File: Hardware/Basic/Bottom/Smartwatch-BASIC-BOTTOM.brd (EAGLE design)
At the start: 33 x 33 mm, 37 parts, among them U1 AD5242-SO16, U3 PCF8523

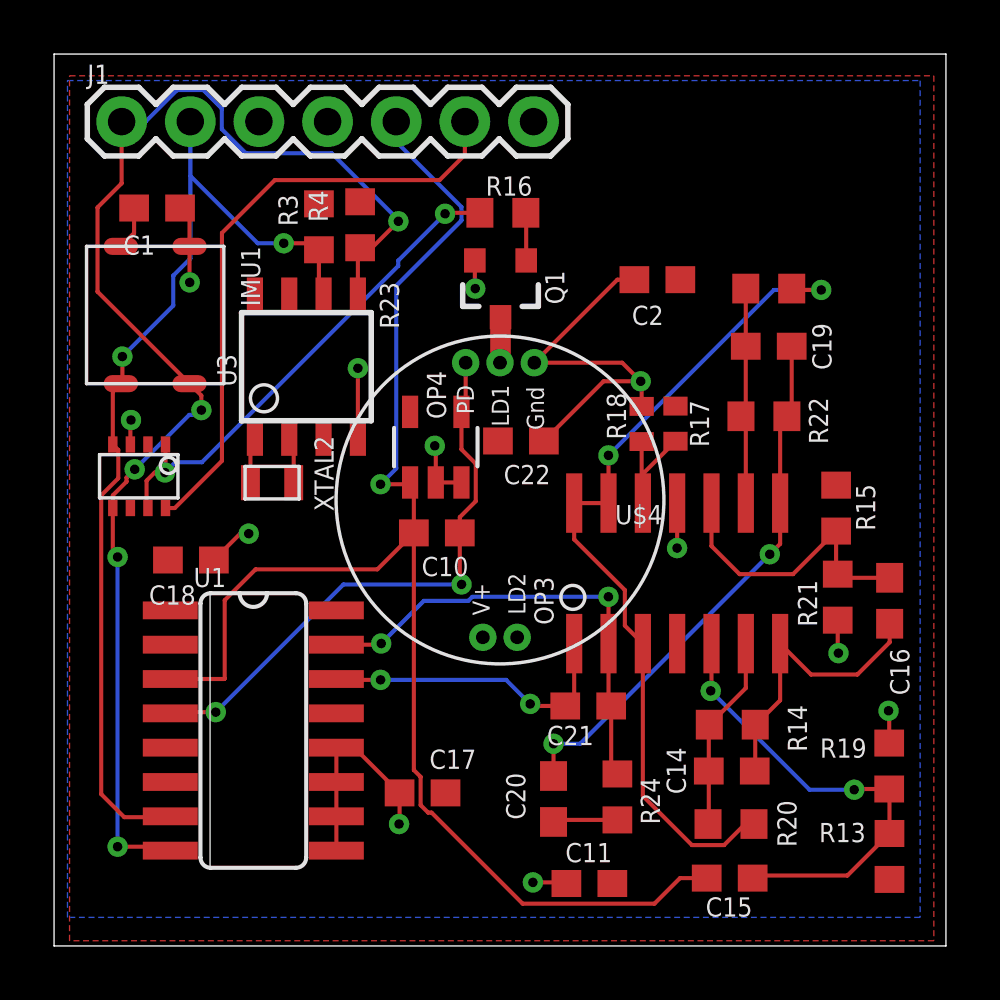
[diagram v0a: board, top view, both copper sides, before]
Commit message: Header Pins Fixed
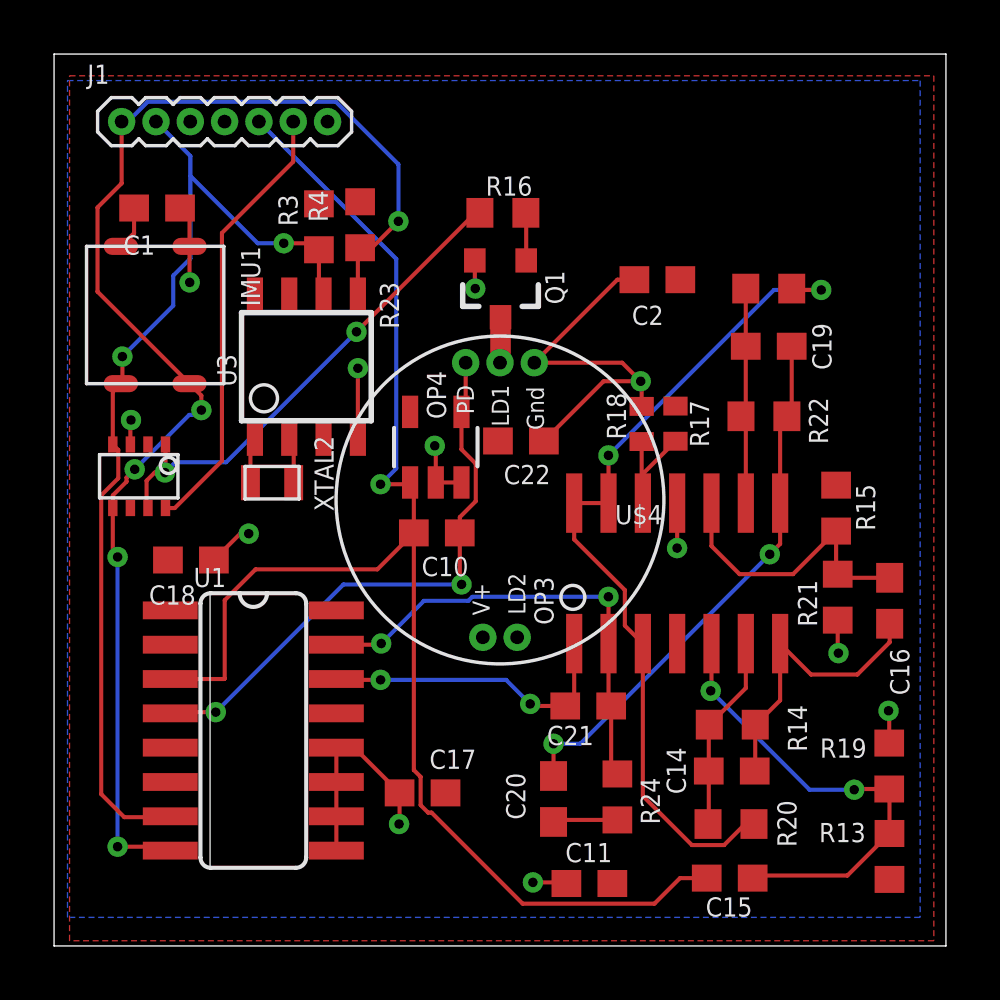
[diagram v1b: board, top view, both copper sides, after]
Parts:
- J1: device LinnesLab-Connectors:1X07 -> LinnesLab-Connectors:1X07_1.27MM
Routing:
- net D26/LED.CTRL: track 22.7 -> 16.5 mm
- net SCL: track 37.0 -> 37.5 mm
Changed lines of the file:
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@@
 <attribute name="VALUE" x="15.3926" y="22.0282" size="0.7112" layer="27" rot="R90"/>
 </element>
-<element name="J1" library="LinnesLab-Connectors" package="1X07" value="" x="5" y="33" smashed="yes">
+<element name="J1" library="LinnesLab-Connectors" package="1X07_1.27MM" value="" x="5" y="33" smashed="yes">
 <attribute name="NAME" x="3.73" y="34.397" size="0.7112" layer="25" font="vector" ratio="20"/>
 <attribute name="VALUE" x="3.73" y="30.968" size="0.6096" layer="27" font="vector" ratio="20"/>
@@
 <wire x1="5.4838" y1="20.13415" x2="7.49845" y2="22.1488" width="0.1524" layer="16"/>
 <wire x1="7.49845" y1="22.1488" x2="7.7724" y2="22.1488" width="0.1524" layer="16"/>
-<wire x1="15.24" y1="29.3116" x2="15.24" y2="29.3624" width="0.1524" layer="16"/>
-<wire x1="15.24" y1="29.3624" x2="12.7708" y2="31.8316" width="0.1524" layer="16"/>
-<wire x1="8.7084" y1="33.48396875" x2="8.02396875" y2="34.1684" width="0.1524" layer="16"/>
-<wire x1="8.02396875" y1="34.1684" x2="7.05603125" y2="34.1684" width="0.1524" layer="16"/>
-<wire x1="5.88763125" y1="33" x2="5" y2="33" width="0.1524" layer="16"/>
-<wire x1="7.05603125" y1="34.1684" x2="5.88763125" y2="33" width="0.1524" layer="16"/>
-<wire x1="9.59603125" y1="31.8316" x2="8.7084" y2="32.71923125" width="0.1524" layer="16"/>
-<wire x1="8.7084" y1="32.71923125" x2="8.7084" y2="33.48396875" width="0.1524" layer="16"/>
-<wire x1="12.7708" y1="31.8316" x2="9.59603125" y2="31.8316" width="0.1524" layer="16"/>
+<wire x1="5" y1="33" x2="5.2282875" y2="33" width="0.1524" layer="16"/>
+<wire x1="5.2282875" y1="33" x2="5.9648875" y2="33.7366" width="0.1524" layer="16"/>
+<wire x1="5.9648875" y1="33.7366" x2="12.9251125" y2="33.7366" width="0.1524" layer="16"/>
+<wire x1="12.9251125" y1="33.7366" x2="15.24" y2="31.4217125" width="0.1524" layer="16"/>
+<wire x1="15.24" y1="31.4217125" x2="15.24" y2="29.3116" width="0.1524" layer="16"/>
 </signal>
 <signal name="SCL">
@@
 <wire x1="6.7676" y1="7.2644" x2="6.7996" y2="7.2964" width="0.1524" layer="1"/>
 <wire x1="7.5438" y1="27.93455" x2="7.5438" y2="30.988" width="0.1524" layer="16"/>
-<wire x1="7.5438" y1="30.988" x2="7.5438" y2="32.9962" width="0.1524" layer="16"/>
-<wire x1="7.5438" y1="32.9962" x2="7.54" y2="33" width="0.1524" layer="16"/>
 <wire x1="10.033" y1="28.4988" x2="7.5438" y2="30.988" width="0.1524" layer="16"/>
 <wire x1="10.033" y1="28.4988" x2="10.9982" y2="28.4988" width="0.1524" layer="16"/>
@@
 <wire x1="12.2238" y1="28.2582" x2="12.3" y2="28.2582" width="0.1524" layer="1"/>
 <wire x1="12.2238" y1="28.2582" x2="11.9832" y2="28.4988" width="0.1524" layer="1"/>
+<wire x1="7.5438" y1="30.988" x2="7.5438" y2="31.7262" width="0.1524" layer="16"/>
+<wire x1="7.5438" y1="31.7262" x2="6.27" y2="33" width="0.1524" layer="16"/>
 </signal>
 <signal name="A6/TIA">
@@
 <wire x1="8.8138" y1="12.3952" x2="8.795" y2="12.3764" width="0.1524" layer="1"/>
 <wire x1="8.795" y1="12.3764" x2="6.7996" y2="12.3764" width="0.1524" layer="1"/>
-<wire x1="15.1638" y1="20.1676" x2="14.5796" y2="19.5834" width="0.1524" layer="16"/>
+<wire x1="14.5796" y1="19.5834" x2="15.1638" y2="20.1676" width="0.1524" layer="16"/>
 <via x="14.5796" y="19.5834" extent="1-16" drill="0.35"/>
-<wire x1="17.574" y1="29.33965" x2="17.574" y2="29.84235" width="0.1524" layer="16"/>
-<wire x1="15.1638" y1="26.92945" x2="15.1638" y2="20.1676" width="0.1524" layer="16"/>
-<wire x1="17.574" y1="29.33965" x2="15.1638" y2="26.92945" width="0.1524" layer="16"/>
 <wire x1="14.5796" y1="19.5834" x2="15.6084" y2="19.5834" width="0.1524" layer="1"/>
 <wire x1="15.6084" y1="19.5834" x2="15.674" y2="19.649" width="0.1524" layer="1"/>
-<wire x1="15.16" y1="32.25635" x2="15.16" y2="33" width="0.1524" layer="16"/>
-<wire x1="17.574" y1="29.84235" x2="15.16" y2="32.25635" width="0.1524" layer="16"/>
+<wire x1="15.1638" y1="27.9162" x2="10.08" y2="33" width="0.1524" layer="16"/>
+<wire x1="15.1638" y1="20.1676" x2="15.1638" y2="27.9162" width="0.1524" layer="16"/>
 </signal>
 <signal name="PD.C">
@@
 <contactref element="U$4" pad="1"/>
 <contactref element="R16" pad="1"/>
-<wire x1="18.2564" y1="29.6258" x2="17.002" y2="29.6258" width="0.1524" layer="1"/>
-<wire x1="17.002" y1="29.6258" x2="16.9672" y2="29.591" width="0.1524" layer="1"/>
-<via x="16.9672" y="29.591" extent="1-16" drill="0.35"/>
 <via x="6.604" y="20.0152" extent="1-16" drill="0.35"/>
-<wire x1="16.9672" y1="29.591" x2="15.2372" y2="27.861" width="0.1524" layer="16"/>
-<wire x1="15.2372" y1="27.861" x2="15.2372" y2="27.66325" width="0.1524" layer="16"/>
-<wire x1="15.2372" y1="27.66325" x2="7.97015" y2="20.3962" width="0.1524" layer="16"/>
-<wire x1="7.97015" y1="20.3962" x2="6.985" y2="20.3962" width="0.1524" layer="16"/>
 <wire x1="6.604" y1="20.0152" x2="6.985" y2="20.3962" width="0.1524" layer="16"/>
 <wire x1="6.604" y1="20.0152" x2="6.6238" y2="20.035" width="0.1524" layer="1"/>
@@
 <wire x1="5.923" y1="19.7152" x2="5.923" y2="18.7532" width="0.1524" layer="1"/>
 <wire x1="5.923" y1="18.7532" x2="5.9738" y2="18.7024" width="0.1524" layer="1"/>
+<wire x1="8.8646" y1="20.3962" x2="13.6906" y2="25.2222" width="0.1524" layer="16"/>
+<via x="13.6906" y="25.2222" extent="1-16" drill="0.35"/>
+<wire x1="6.985" y1="20.3962" x2="8.8646" y2="20.3962" width="0.1524" layer="16"/>
+<wire x1="13.6906" y1="25.2222" x2="18.0942" y2="29.6258" width="0.1524" layer="1"/>
+<wire x1="18.0942" y1="29.6258" x2="18.2564" y2="29.6258" width="0.1524" layer="1"/>
 </signal>
 <signal name="N$10">
@@
 <contactref element="J1" pad="6"/>
 <contactref element="U$4" pad="8"/>
-<wire x1="17.7" y1="33" x2="17.7" y2="31.7716" width="0.1524" layer="1"/>
-<wire x1="17.7" y1="31.7716" x2="16.764" y2="30.8356" width="0.1524" layer="1"/>
-<wire x1="16.764" y1="30.8356" x2="10.668" y2="30.8356" width="0.1524" layer="1"/>
-<wire x1="10.668" y1="30.8356" x2="8.7122" y2="28.8798" width="0.1524" layer="1"/>
-<wire x1="8.7122" y1="28.8798" x2="8.7122" y2="20.447" width="0.1524" layer="1"/>
+<wire x1="8.7122" y1="20.447" x2="8.7122" y2="28.8798" width="0.1524" layer="1"/>
 <wire x1="8.7122" y1="20.447" x2="6.9676" y2="18.7024" width="0.1524" layer="1"/>
 <wire x1="6.9676" y1="18.7024" x2="6.6238" y2="18.7024" width="0.1524" layer="1"/>
+<wire x1="11.35" y1="31.5176" x2="11.35" y2="33" width="0.1524" layer="1"/>
+<wire x1="8.7122" y1="28.8798" x2="11.35" y2="31.5176" width="0.1524" layer="1"/>
 </signal>
 </signals>

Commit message: GPS Removed, added back original display, kept pads for adafruit display
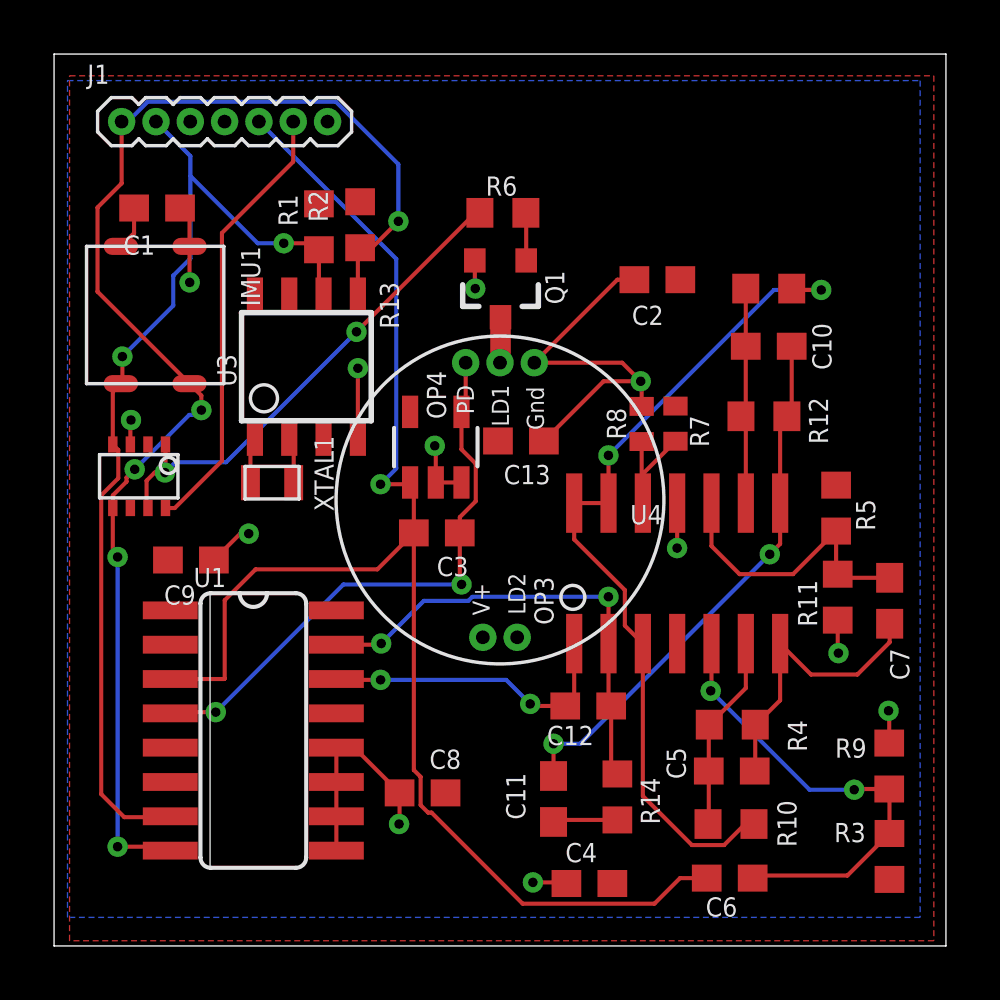
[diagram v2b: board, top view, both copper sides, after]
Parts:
- removed C19: 2.2n, LinnesLab-Passives:C0603
- removed C20: 22u, LinnesLab-Passives:C0603
- removed R23: 1M, LinnesLab-Passives:R0603
- removed R24: 10k, LinnesLab-Passives:R0603
- added C3, C4: 100n, LinnesLab-Passives:C0603
- added R1, R2: 10k, LinnesLab-Passives:R0603
- C10: value 100n -> 2.2n
- C11: value 100n -> 22u
- R13: value 220k -> 1M
- R14: value 10M -> 10k
- R3: value 10k -> 220k
- R4: value 10k -> 10M
- moved R3 31.4 mm to (33.4, 5.81), turned to 270 degrees
- moved R4 23.1 mm to (27.6, 10.7), turned to 0 degrees
- moved R13 21.5 mm to (28.9, 26.8), turned to 180 degrees
- moved C10 14.1 mm to (28.9, 24.7)
- moved R14 5.02 mm to (23.3, 8.01), turned to 270 degrees
- moved C11 3.40 mm to (21.0, 7.94), turned to 270 degrees
- renumbered C14 to C5, C15 to C6, C16 to C7, C17 to C8, C18 to C9, C21 to C12, C22 to C13, R15 to R5, R16 to R6, R17 to R7, R18 to R8, R19 to R9, R20 to R10, R21 to R11, R22 to R12, U$3 to U2, U$4 to U4, XTAL2 to XTAL1
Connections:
- net 3.3V: now also C4.2, R1.2, R2.2; no longer C11.2, R13.2, R4.2
- net A6/TIA: now also C3.2; no longer C10.2
- net G.W2: now also R14.1; no longer R24.1
- net GND: now also C4.1; no longer C11.1
- net N$13: now also R3.1; no longer R13.1
- net N$15: now also R4.1; no longer R14.1
- net N$16: now also R4.2; no longer R14.2
- net N$18: now also C10.2, R13.2; no longer C19.2, R23.2
- net N$19: now also C10.1, C11.1; no longer C19.1, C20.1
- net N$20: now also C11.2, R14.2; no longer C20.2, R24.2
- net PD.C: now also C3.1; no longer C10.1
- net SCL: now also R1.1; no longer R3.1
- net SDA: now also R2.1; no longer R4.1
- net VREF: now also R13.1; no longer R23.1
